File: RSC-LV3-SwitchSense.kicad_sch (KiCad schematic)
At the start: 0 parts

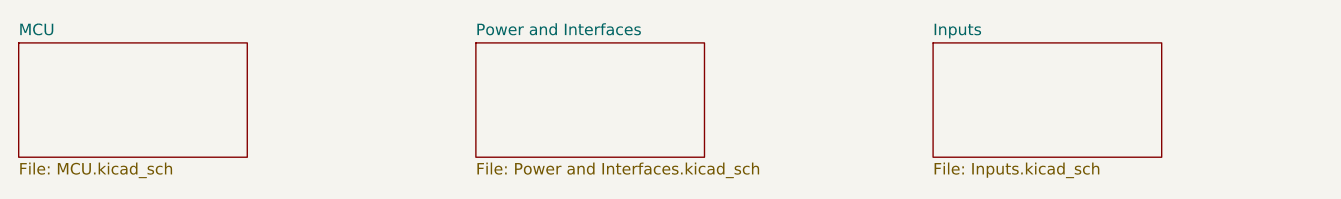
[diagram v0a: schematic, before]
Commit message: updated pinout, begin layout
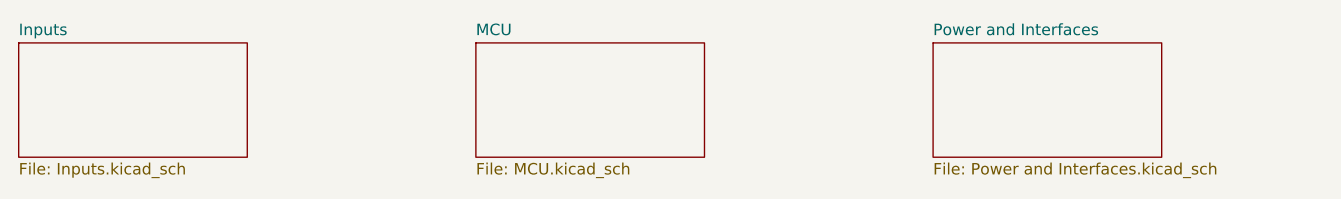
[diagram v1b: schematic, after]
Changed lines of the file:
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@@
 	(paper "A4")
-	(sheet
-		(at 38.1 38.1)
-		(size 25.4 12.7)
-		(exclude_from_sim no)
-		(in_bom yes)
-		(on_board yes)
-		(dnp no)
-		(fields_autoplaced yes)
-		(stroke
-			(width 0.1524)
-			(type solid)
-		)
-		(fill
-			(color 0 0 0 0)
-		)
-		(property "Sheetname" "MCU"
-			(at 38.1 37.3884 0)
-			(show_name no)
-			(do_not_autoplace no)
-			(effects
-				(font
-					(size 1.27 1.27)
-				)
-				(justify left bottom)
-			)
-		)
-		(property "Sheetfile" "MCU.kicad_sch"
-			(at 38.1 51.3846 0)
-			(show_name no)
-			(do_not_autoplace no)
-			(effects
-				(font
-					(size 1.27 1.27)
-				)
-				(justify left top)
-			)
-		)
-		(instances
-			(project "RSC-LV3-SwitchSense"
-				(path "/ea09e839-df61-4c3f-abdc-aa7ae2f772fe"
-					(page "2")
-				)
-			)
-		)
-	)
 	(sheet
 		(at 88.9 38.1)
@@
 			(color 0 0 0 0)
 		)
-		(property "Sheetname" "Power and Interfaces"
+		(property "Sheetname" "MCU"
 			(at 88.9 37.3884 0)
 			(show_name no)
@@
 			)
 		)
-		(property "Sheetfile" "Power and Interfaces.kicad_sch"
+		(property "Sheetfile" "MCU.kicad_sch"
 			(at 88.9 51.3846 0)
 			(show_name no)
@@
 			(project "RSC-LV3-SwitchSense"
 				(path "/ea09e839-df61-4c3f-abdc-aa7ae2f772fe"
-					(page "5")
+					(page "3")
 				)
 			)
@@
 			(color 0 0 0 0)
 		)
-		(property "Sheetname" "Inputs"
+		(property "Sheetname" "Power and Interfaces"
 			(at 139.7 37.3884 0)
 			(show_name no)
@@
 			)
 		)
-		(property "Sheetfile" "Inputs.kicad_sch"
+		(property "Sheetfile" "Power and Interfaces.kicad_sch"
 			(at 139.7 51.3846 0)
 			(show_name no)
@@
 			(project "RSC-LV3-SwitchSense"
 				(path "/ea09e839-df61-4c3f-abdc-aa7ae2f772fe"
-					(page "7")
+					(page "6")
 				)
 			)
+		)
+	)
+	(sheet
+		(at 38.1 38.1)
+		(size 25.4 12.7)
+		(exclude_from_sim no)
+		(in_bom yes)
+		(on_board yes)
+		(dnp no)
+		(fields_autoplaced yes)
+		(stroke
+			(width 0.1524)
+			(type solid)
+		)
+		(fill
+			(color 0 0 0 0)
+		)
+		(property "Sheetname" "Inputs"
+			(at 38.1 37.3884 0)
+			(show_name no)
+			(do_not_autoplace no)
+			(effects
+				(font
+					(size 1.27 1.27)
+				)
+				(justify left bottom)
+			)
+		)
+		(property "Sheetfile" "Inputs.kicad_sch"
+			(at 38.1 51.3846 0)
+			(show_name no)
+			(do_not_autoplace no)
+			(effects
+				(font
+					(size 1.27 1.27)
+				)
+				(justify left top)
+			)
+		)
+		(instances
+			(project "RSC-LV3-SwitchSense"
+				(path "/ea09e839-df61-4c3f-abdc-aa7ae2f772fe"
+					(page "2")
+				)
+			)
